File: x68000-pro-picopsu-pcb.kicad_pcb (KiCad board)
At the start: 2 copper layers, 209 x 98 mm, 27 parts, among them J1 Fan Header, J2 Screw_Terminal_01x07, J3 Screw_Terminal_01x07, J4 PicoPSU, U1 74LS04

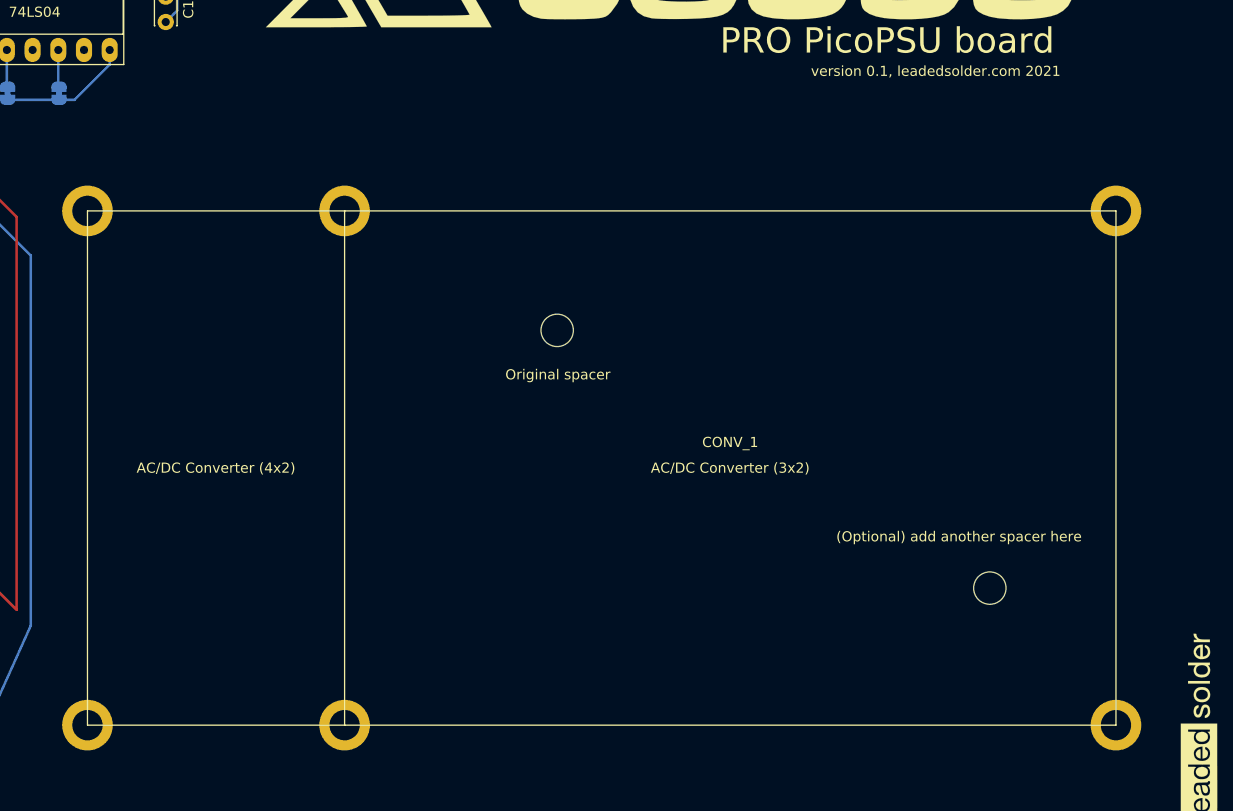
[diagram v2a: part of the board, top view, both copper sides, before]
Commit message: mounting holes fixed
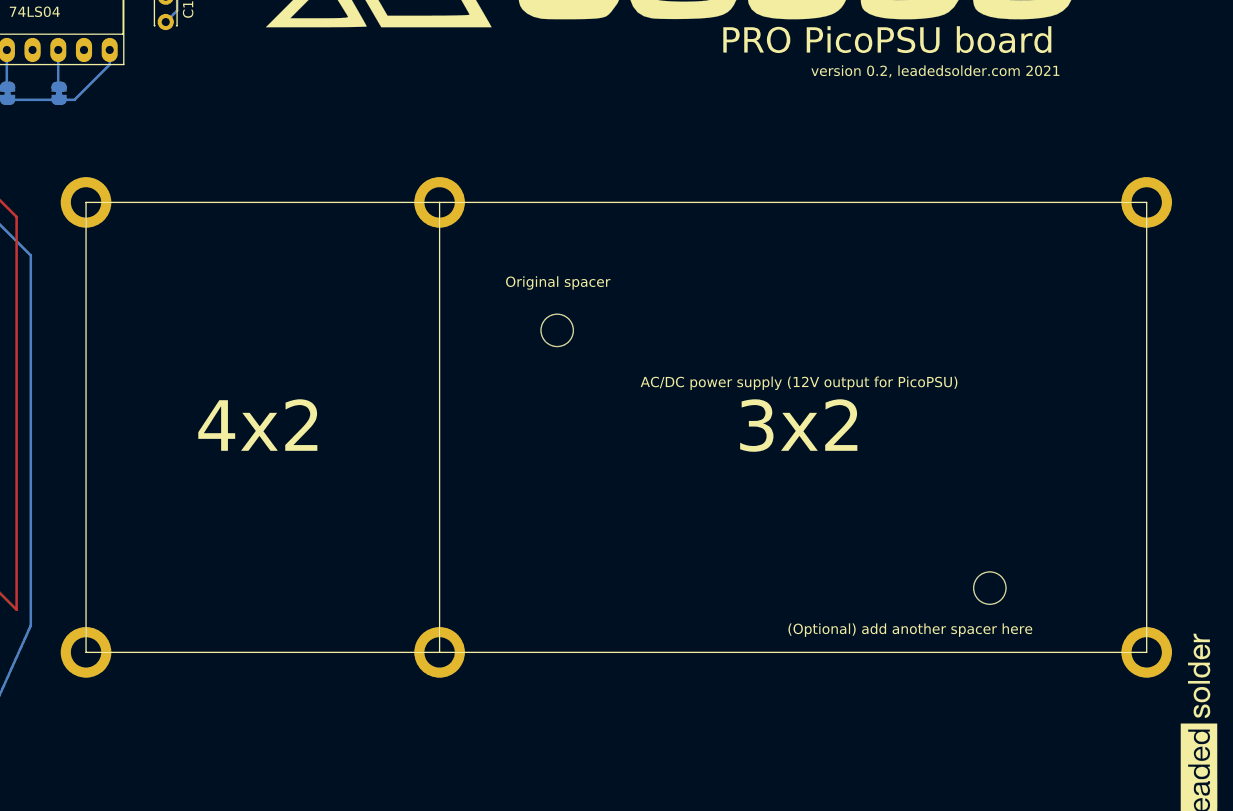
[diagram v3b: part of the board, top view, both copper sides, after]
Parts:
- moved CONV_1 79.6 mm to (221.2, 130.8)
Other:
- board text added: "special thanks: mattsoft for the x68000 og picopsu board dave park for advice on PCB design and safety"
- board text added: "version 0.2, leadedsolder.com 2021"
- board text removed: "special thanks: mattsoft for the x68000 og picopsu board"
- board text removed: "version 0.1, leadedsolder.com 2021"
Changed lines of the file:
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@@
       (effects (font (size 1 1) (thickness 0.15)))
     )
+    (fp_circle (center 0 0) (end 3.45 0) (layer F.CrtYd) (width 0.05))
+    (fp_circle (center 0 0) (end 3.2 0) (layer Cmts.User) (width 0.15))
     (fp_text user %R (at 0.3 0) (layer F.Fab)
       (effects (font (size 1 1) (thickness 0.15)))
     )
-    (fp_circle (center 0 0) (end 3.2 0) (layer Cmts.User) (width 0.15))
-    (fp_circle (center 0 0) (end 3.45 0) (layer F.CrtYd) (width 0.05))
     (pad 1 np_thru_hole circle (at 0 0) (size 3.2 3.2) (drill 3.2) (layers *.Cu *.Mask))
   )
@@
   )
   (module OffboardACDC:3x2_4x2 (layer F.Cu)
-    (at 142 138 180)
-    (fp_text reference CONV_1 (at -38.1 27.94) (layer F.SilkS)
+    (at 221.234 130.81 180)
+    (fp_text reference CONV_1 (at -38.1 27.94) (layer F.SilkS) hide
       (effects (font (size 1 1) (thickness 0.15)))
     )
@@
       (effects (font (size 1 1) (thickness 0.15)))
     )
-    (fp_text user "AC/DC Converter (3x2)" (at -38.1 25.4) (layer F.SilkS)
-      (effects (font (size 1 1) (thickness 0.15)))
-    )
-    (fp_text user "AC/DC Converter (4x2)" (at 12.7 25.4) (layer F.SilkS)
-      (effects (font (size 1 1) (thickness 0.15)))
-    )
-    (fp_line (start 25.4 50.8) (end 0 50.8) (layer F.SilkS) (width 0.12))
-    (fp_line (start 25.4 0) (end 25.4 50.8) (layer F.SilkS) (width 0.12))
-    (fp_line (start 0 0) (end 25.4 0) (layer F.SilkS) (width 0.12))
-    (fp_line (start -76.2 0) (end 0 0) (layer F.SilkS) (width 0.12))
-    (fp_line (start -76.2 50.8) (end -76.2 0) (layer F.SilkS) (width 0.12))
-    (fp_line (start 0 50.8) (end -76.2 50.8) (layer F.SilkS) (width 0.12))
-    (fp_line (start 0 0) (end 0 50.8) (layer F.SilkS) (width 0.12))
-    (pad 1 thru_hole circle (at 25.4 0 180) (size 5 5) (drill 3) (layers *.Cu *.Mask)
-      (net 2 /PSU_COM))
-    (pad 1 thru_hole circle (at 25.4 50.8 180) (size 5 5) (drill 3) (layers *.Cu *.Mask)
-      (net 2 /PSU_COM))
-    (pad 1 thru_hole circle (at -76.2 0 180) (size 5 5) (drill 3) (layers *.Cu *.Mask)
-      (net 2 /PSU_COM))
-    (pad 1 thru_hole circle (at -76.2 50.8 180) (size 5 5) (drill 3) (layers *.Cu *.Mask)
-      (net 2 /PSU_COM))
-    (pad 1 thru_hole circle (at 0 50.8 180) (size 5 5) (drill 3) (layers *.Cu *.Mask)
+    (fp_text user "AC/DC power supply (12V output for PicoPSU)" (at 34.29 26.67) (layer F.SilkS)
+      (effects (font (size 1 1) (thickness 0.15)))
+    )
+    (fp_text user 3x2 (at 34.29 22.225) (layer F.SilkS)
+      (effects (font (size 5 5) (thickness 0.15)))
+    )
+    (fp_text user 4x2 (at 87.63 22.225) (layer F.SilkS)
+      (effects (font (size 5 5) (thickness 0.15)))
+    )
+    (fp_line (start 104.775 44.45) (end 69.85 44.45) (layer F.SilkS) (width 0.12))
+    (fp_line (start 104.775 0) (end 104.775 44.45) (layer F.SilkS) (width 0.12))
+    (fp_line (start 69.85 0) (end 104.775 0) (layer F.SilkS) (width 0.12))
+    (fp_line (start 0 0) (end 69.85 0) (layer F.SilkS) (width 0.12))
+    (fp_line (start 0 44.45) (end 0 0) (layer F.SilkS) (width 0.12))
+    (fp_line (start 69.85 44.45) (end 0 44.45) (layer F.SilkS) (width 0.12))
+    (fp_line (start 69.85 0) (end 69.85 44.45) (layer F.SilkS) (width 0.12))
+    (fp_text user "69.85 x 44.45" (at 17.78 8.89) (layer Dwgs.User)
+      (effects (font (size 1 1) (thickness 0.15)))
+    )
+    (fp_text user "AC/DC Converter (3x2)" (at -117.334 32.59) (layer F.SilkS) hide
+      (effects (font (size 1 1) (thickness 0.15)))
+    )
+    (fp_text user "AC/DC Converter (4x2)" (at -66.534 32.59) (layer F.SilkS) hide
+      (effects (font (size 1 1) (thickness 0.15)))
+    )
+    (pad 1 thru_hole circle (at 104.775 0 180) (size 5 5) (drill 3) (layers *.Cu *.Mask)
+      (net 2 /PSU_COM))
+    (pad 1 thru_hole circle (at 104.775 44.45 180) (size 5 5) (drill 3) (layers *.Cu *.Mask)
+      (net 2 /PSU_COM))
+    (pad 1 thru_hole circle (at 0 44.45 180) (size 5 5) (drill 3) (layers *.Cu *.Mask)
+      (net 2 /PSU_COM))
+    (pad 1 thru_hole circle (at 69.85 44.45 180) (size 5 5) (drill 3) (layers *.Cu *.Mask)
+      (net 2 /PSU_COM))
+    (pad 1 thru_hole circle (at 69.85 0 180) (size 5 5) (drill 3) (layers *.Cu *.Mask)
       (net 2 /PSU_COM))
     (pad 1 thru_hole circle (at 0 0 180) (size 5 5) (drill 3) (layers *.Cu *.Mask)
@@
   (gr_line (start 98.298 97.028) (end 98.298 139.446) (layer F.SilkS) (width 0.12))
   (gr_line (start 88.646 97.028) (end 98.298 97.028) (layer F.SilkS) (width 0.12))
-  (gr_text "special thanks:\nmattsoft for the x68000 og picopsu board" (at 193.548 57.658) (layer B.SilkS)
+  (gr_text "special thanks:\nmattsoft for the x68000 og picopsu board\ndave park for advice on PCB design and safety" (at 193.548 57.658) (layer B.SilkS)
     (effects (font (size 1 1) (thickness 0.15)) (justify mirror))
   )
@@
     (effects (font (size 1 1) (thickness 0.15)) (justify mirror))
   )
-  (gr_text "Original spacer" (at 163.068 103.378) (layer F.SilkS)
+  (gr_text "Original spacer" (at 163.068 94.234) (layer F.SilkS)
     (effects (font (size 1 1) (thickness 0.15)))
   )
-  (gr_text "(Optional) add another spacer here" (at 202.692 119.38) (layer F.SilkS)
+  (gr_text "(Optional) add another spacer here" (at 197.866 128.524) (layer F.SilkS)
     (effects (font (size 1 1) (thickness 0.15)))
   )
@@
     (effects (font (size 2.5 2.5) (thickness 0.15)))
   )
-  (gr_text "version 0.1, leadedsolder.com 2021" (at 200.4 73.4) (layer F.SilkS)
+  (gr_text "version 0.2, leadedsolder.com 2021" (at 200.4 73.4) (layer F.SilkS)
     (effects (font (size 1 1) (thickness 0.15)))
   )

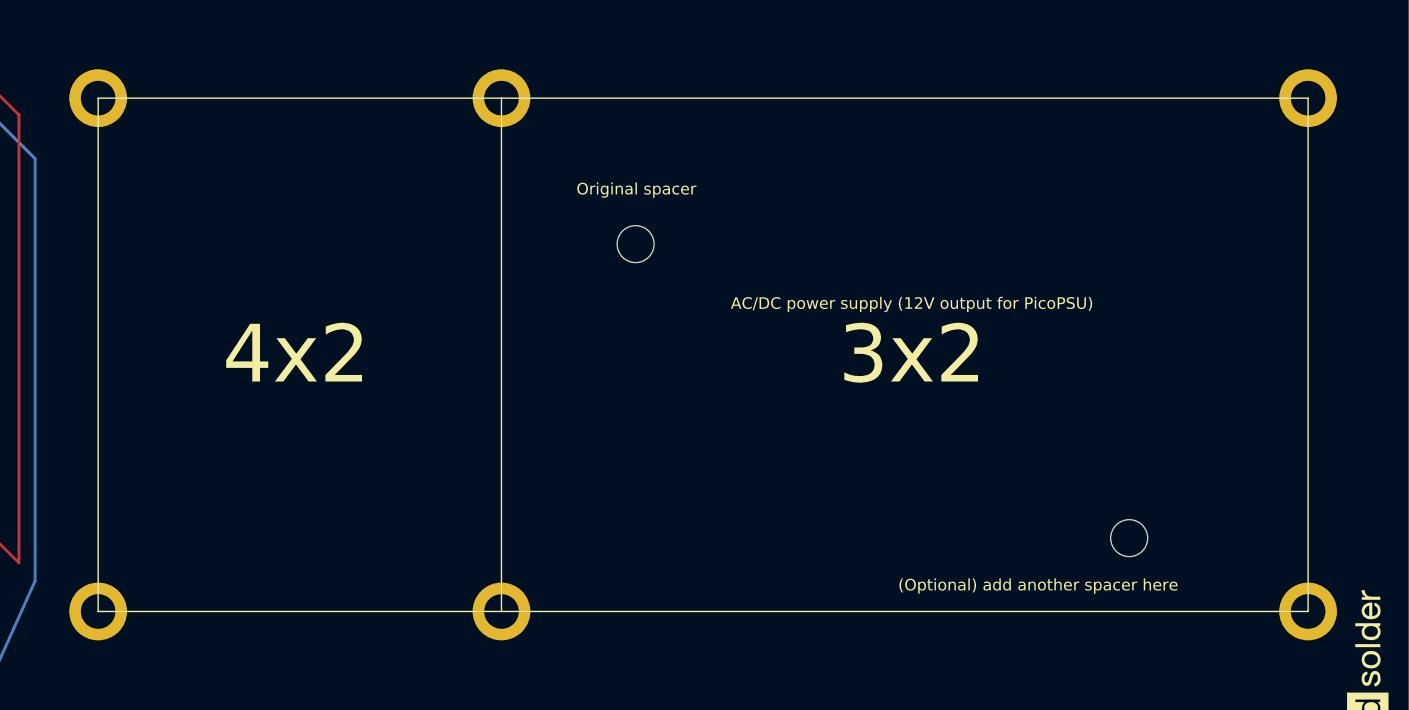
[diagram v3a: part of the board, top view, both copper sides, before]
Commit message: Tweak converter a bit backward, in case they use a 4x2
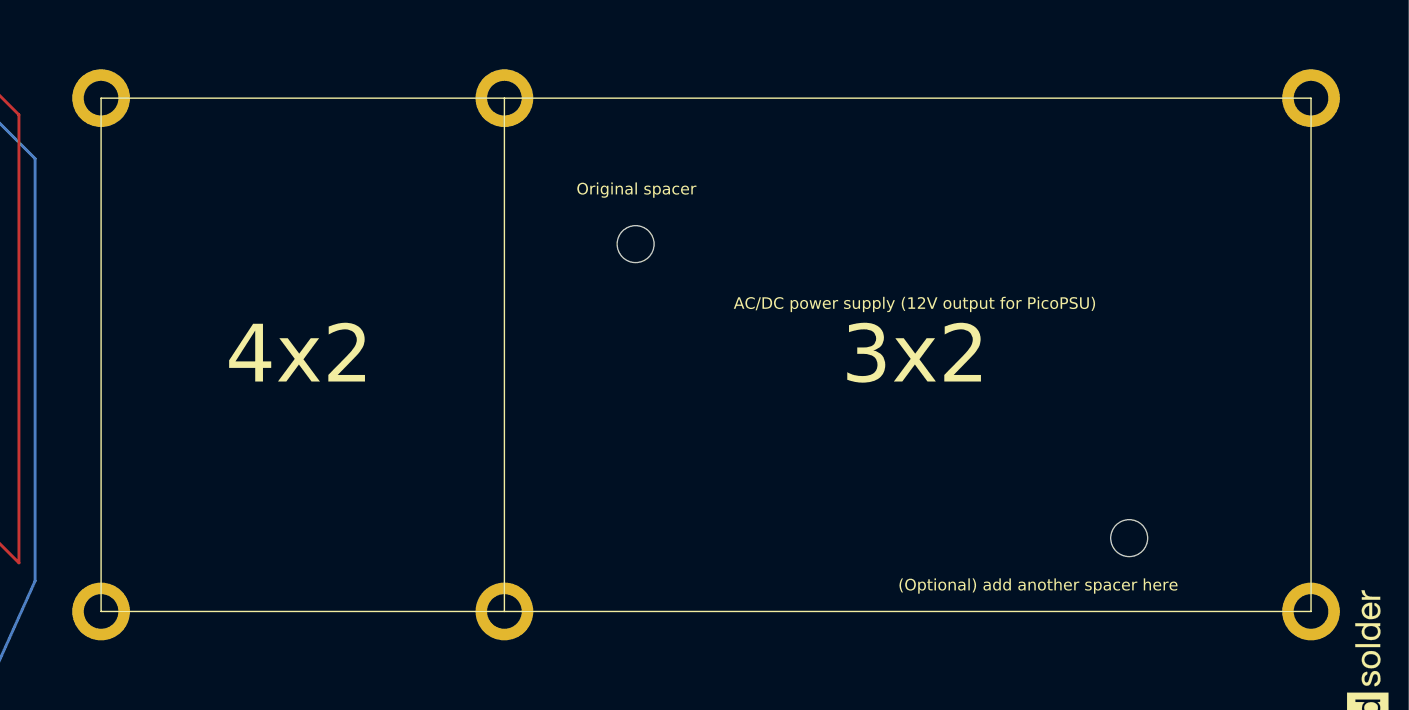
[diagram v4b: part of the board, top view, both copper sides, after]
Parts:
- moved CONV_1 0.25 mm to (221.5, 130.8)
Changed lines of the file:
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@@
   )
   (module OffboardACDC:3x2_4x2 (layer F.Cu)
-    (at 221.234 130.81 180)
+    (at 221.488 130.81 180)
     (fp_text reference CONV_1 (at -38.1 27.94) (layer F.SilkS) hide
       (effects (font (size 1 1) (thickness 0.15)))
